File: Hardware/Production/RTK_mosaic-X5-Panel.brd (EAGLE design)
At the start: 151.8 x 101.6 mm, 350 parts, among them J2 MAGJACK-POE, J3 MICRO-SD-PUSH-PUSH-EXT-PIN, J4 Vertical Qwiic Connector, J9 MAGJACK-POE, U1 ESP32-WROVER-IE, U10 POE_PSU-DP990X, U11 SN74AVC4T774PW, U17 URB2405YMD, U2 CH340C, U3 XC6222B331MR-G, U4 TXS0108, U5 TXS0108, U6 XC6222B331MR-G, U7 KSZ8041NL, U8 MOSAIC-X5X5, U9 KSZ8041NL

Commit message: Tweaked and panelized
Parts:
- removed ACT, ACT2: JUMPER-SMT_2_NC_TRACE_SILK, SparkFun-Jumpers:SMT-JUMPER_2_NC_TRACE_SILK
- removed FRAME1: FRAME-LEDGER, SparkFun-Aesthetics:CREATIVE_COMMONS
- removed FRAME3: FRAME-LEDGERNO_FOOTPRINT, SparkFun-Aesthetics:DUMMY
- removed LOGO1: SPECIAL_INSTRUCTIONS-ORDERING, SparkFun-Aesthetics:ORDERING_INSTRUCTIONS
- removed U$100: (no value), output:MOSAIC_X50
- removed U$4: (no value), output:#LINK#1
- removed U$9: (no value), output:#ACT#0
- added E$1, E$2, E$3, E$4: (no value), SparkFun-Aesthetics:FIDUCIAL-1X2
- added E$5, E$6: (no value), SparkFun-Retired:FIDUCIAL-1.5X3
- added SPEED, SPEED2: JUMPER-SMT_2_NC_TRACE_SILK, SparkFun-Jumpers:SMT-JUMPER_2_NC_TRACE_SILK
- added U$109: (no value), output:#_BT_#1
- added U$110, U$116: (no value), output:#_LOG_#5
- added U$111: (no value), output:#_PVT_#3
- added U$112: (no value), output:#_RTK_#4
- added U$115: (no value), output:#_WIFI_#2
- added U$117: (no value), output:#_#RESET#_#0
- added U$118: (no value), output:#_BOOT_#1
- added U$119: (no value), output:#MOSAIC#8
- added U$120: (no value), output:#LINK#1
- added U$121, U$122: (no value), output:#SPEED#0
- U$2: device output:#ACT#0 -> output:MOSAIC#X50
- U$69, U$99: device output:RTK_MOSAIC_X50 -> output:RTK_MOSAIC#X50
- U3, U6: value XC6222B331MR-G -> AP7361C-33FGEUDFN-8; device SparkFun-IC-Power:SOT23-5 -> SparkFun-IC-Power:UDFN-8
- U8: device Septentrio_Mosaic:MOSAIC_LGA -> Septentrio_mosaic-X5:MOSAIC_LGA
- moved U$2 53.5 mm to (64.2, 97.0), flipped to the top, turned to 90 degrees
- moved U$10 11.9 mm to (131.6, 100.1)
- moved LINK 11.0 mm to (131.5, 98.4)
- moved LINK2 11.0 mm to (9.59, 98.4)
- moved U3 1.93 mm to (70.8, 45.1), turned to 90 degrees
- moved U6 1.93 mm to (70.8, 40.0), turned to 90 degrees
- moved FB3 1.43 mm to (60.6, 73.8)
- moved R39 1.31 mm to (35.2, 14.0)
- moved R36 1.31 mm to (10.5, 14.0)
- moved R28 1.31 mm to (18.7, 14.0)
- moved R38 1.31 mm to (27.0, 14.0)
- moved R27 1.31 mm to (52.4, 14.0)
- moved R37 1.31 mm to (43.5, 14.0)
- moved U$97 1.31 mm to (51.0, 66.9)
- moved D10 0.32 mm to (131.8, 11.4)
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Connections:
- net ACT_ESP32 renamed SPEED_ESP32
- net ACT_MOSAIC renamed SPEED_MOSAIC
- net N$13 renamed ESP32_RF
- removed net ACT: ACT.1, J9.14
- removed net ACT2: ACT2.1, J2.14
- removed net LINK: J9.12, LINK.1
- removed net LINK2: J2.12, LINK2.1
- new net N$3: J9.14, LINK.1
- new net N$40: J2.14, LINK2.1
- new net N$41: J2.12, SPEED2.1
- new net N$7: J9.12, SPEED.1
- net 3.3V: now also U6.1; no longer U6.5
- net 3.3V_SW: now also U3.1; no longer U3.5
- net 5V: now also U3.5, U3.8, U6.5, U6.8; no longer U3.1, U3.3, U6.1, U6.3
- net GND: now also U3.4, U3.EP, U6.4, U6.EP; no longer U3.2, U6.2
- net N$12: now also SPEED.2; no longer ACT.2
- net N$142: now also SPEED2.2; no longer ACT2.2
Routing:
- net N$143: track 21.7 -> 36.0 mm
- net N$21: track 41.5 -> 30.1 mm
- net N$12: track 29.8 -> 40.3 mm
- net N$142: track 34.1 -> 25.3 mm
- net GND: track 8.92 -> 17.6 mm, vias 204 -> 330
- net CH340-TXO: track 57.1 -> 60.8 mm
- net N$7: track 0.00 -> 3.32 mm
- net N$3: track 0.00 -> 3.30 mm
- net ACT: track 3.30 -> 0.00 mm
- net LINK: track 3.25 -> 0.00 mm
- net MOSAIC_LOG_BTN_IO: track 148.9 -> 151.7 mm
- net LINK2: track 2.48 -> 0.00 mm
- net N$40: track 0.00 -> 2.48 mm
- net N$41: track 0.00 -> 2.46 mm
- net ACT2: track 2.43 -> 0.00 mm
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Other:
- board size 151.8 x 101.6 mm -> 165.5 x 131.1 mm
- board text added: "Route Out"
- board text added: "v-score"
- board text removed: "Controlled Impedance: JLC7628 Material: TG155 4-Layers Thickness: 1.6mm Outer Copper: 1oz Inner Copper: 0.5oz Finish: ENIG Red Solder Resist White Silkscreen No clean process"
- board text removed: "Dimensions In Inches"
- board text removed: "Paul Clark"
- board text removed: "V-Score To V-Score"

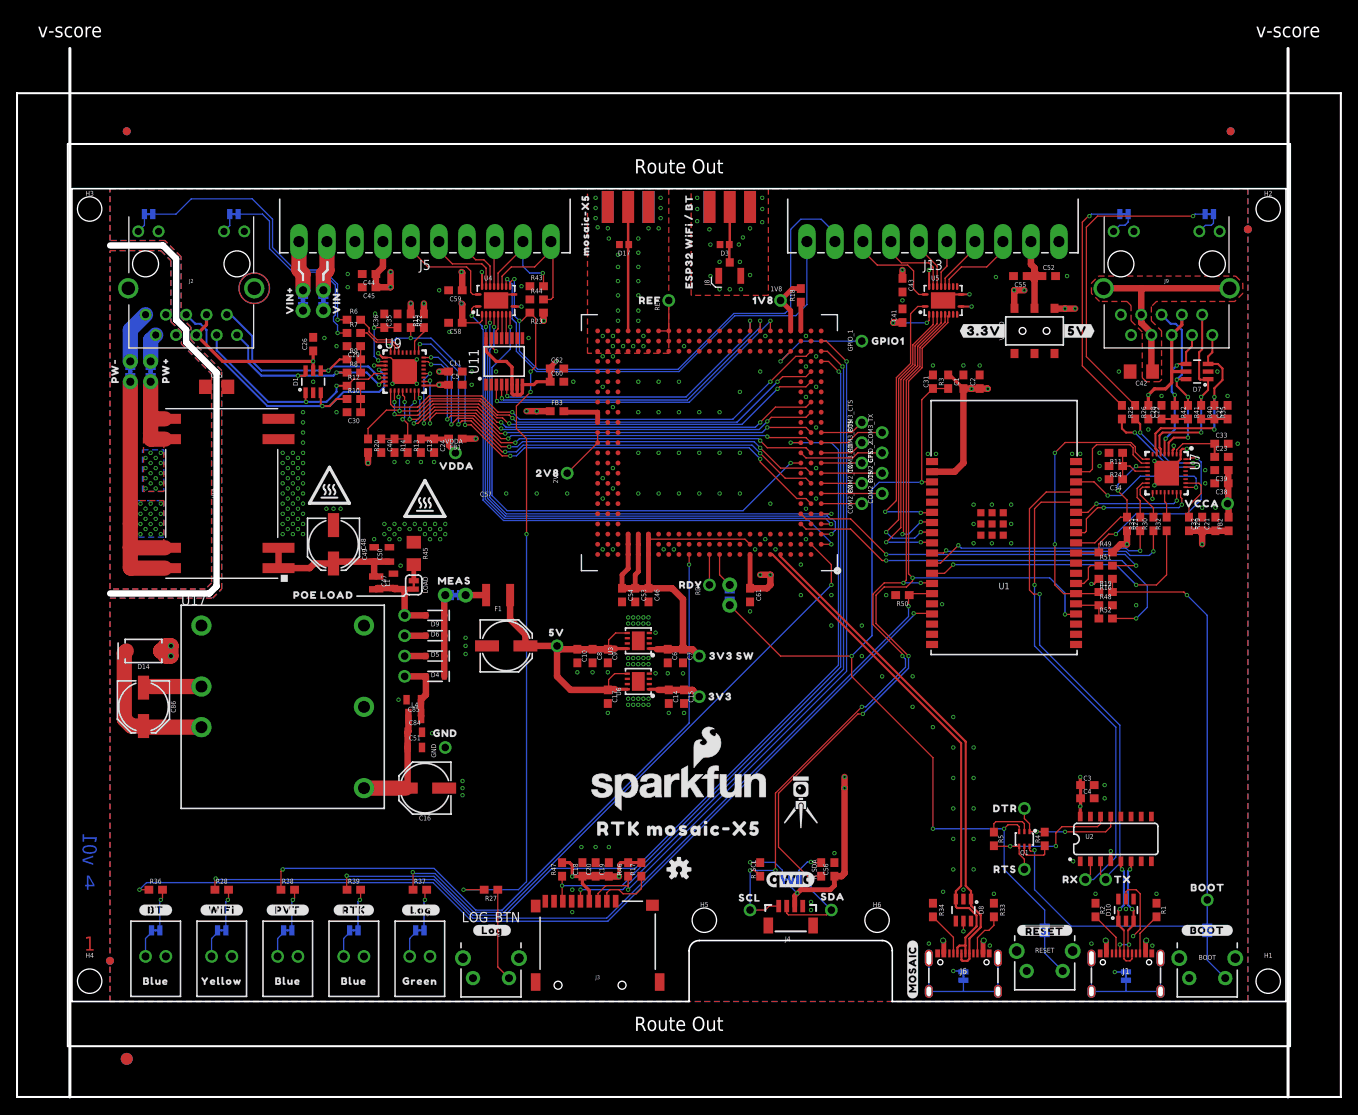
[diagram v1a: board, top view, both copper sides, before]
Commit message: Adding u.FL connector for mosaic-H - with standoff holes for a u.FL-SMA daughter board
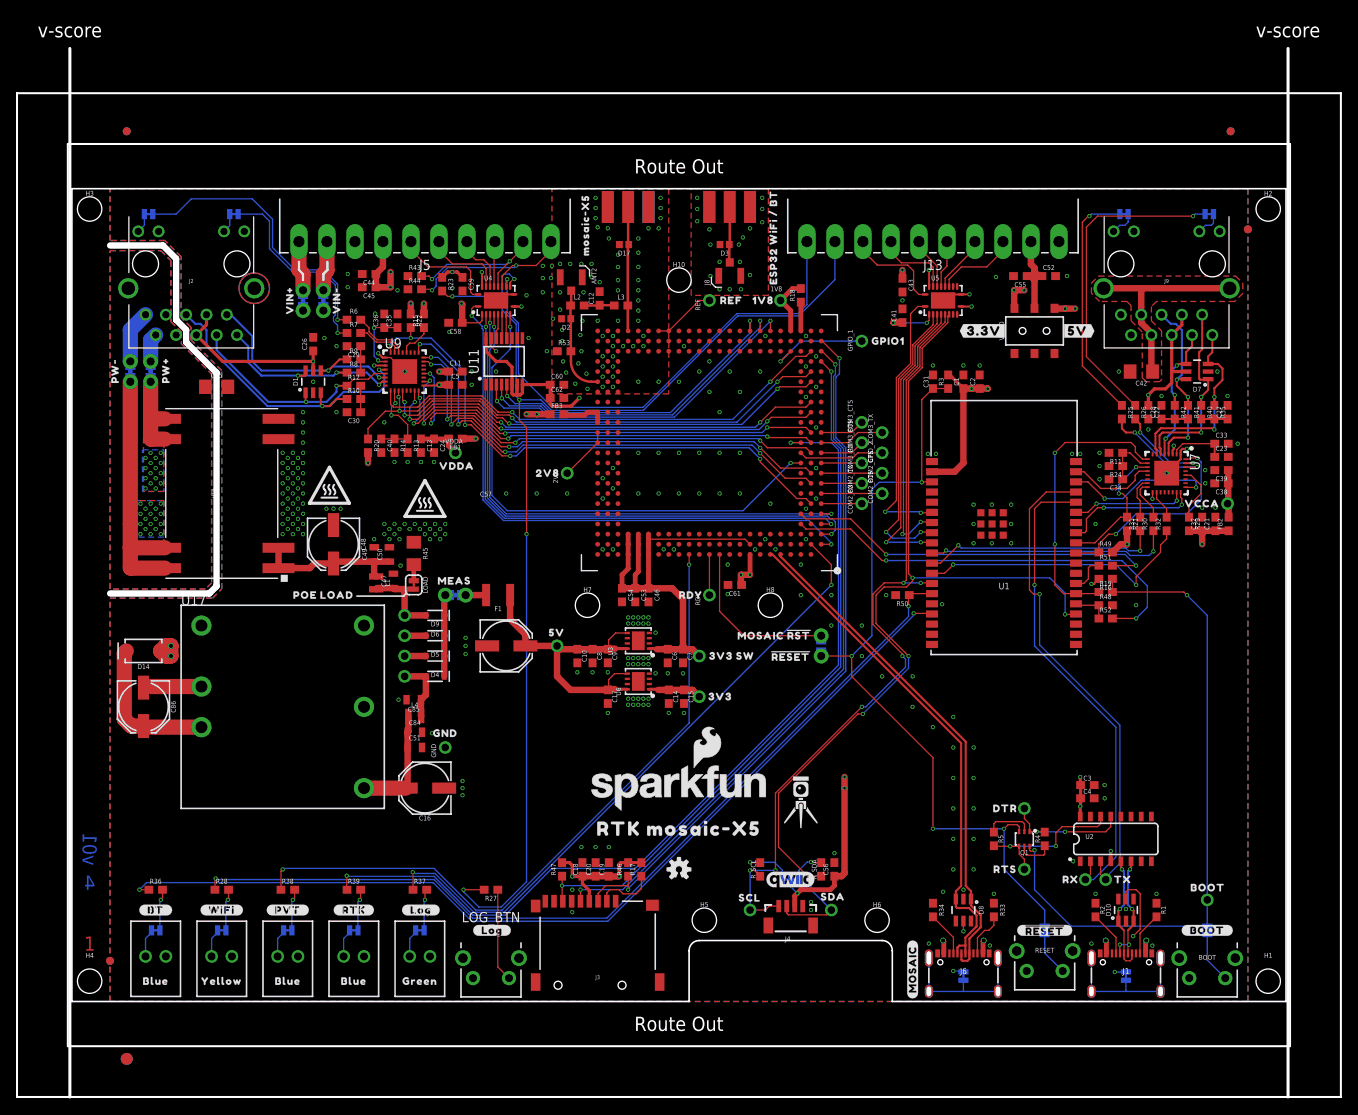
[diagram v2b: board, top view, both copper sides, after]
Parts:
- added ANT2: DNP, SparkFun-Connectors:U.FL_REDUCED_FOOTPRINT__NO_CREAM
- added C12: DNP, SparkFun-Capacitors:0603_NO_CREAM
- added D2: PESD0402, SparkFun-DiscreteSemi:0402
- added H10, H7, H8: STAND-OFFTIGHT, SparkFun-Hardware:STAND-OFF-TIGHT
- added L2, L3: DNP, SparkFun-Coils:0603_NO-CREAM
- added R53: 0, SparkFun-Resistors:0603
- added U$4: (no value), output:#RESET#0
- added U$9: (no value), output:MOSAIC_#RST#6
- U7, U9: device Septentrio_Mosaic:MLF55Q-32LD -> Septentrio_mosaic-X5:MLF55Q-32LD
- moved R43 15.3 mm to (42.9, 90.7)
- moved R44 15.3 mm to (42.9, 89.0)
- moved MOSAIC_RST 13.1 mm to (93.7, 44.5)
- moved R23 12.3 mm to (46.3, 89.7), turned to 270 degrees
- moved U$21 10.6 mm to (87.7, 102.1)
- moved U$79 10.2 mm to (84.5, 87.6)
- moved U$74 7.41 mm to (89.9, 43.2)
- moved U$73 6.35 mm to (82.6, 45.8)
- moved REF 5.08 mm to (79.7, 87.6)
- moved U$80 5.08 mm to (77.5, 86.1)
- moved C62 3.68 mm to (60.6, 75.4)
- moved C61 2.29 mm to (82.9, 52.1), turned to 180 degrees
- moved RDY 1.27 mm to (79.7, 50.8)
- moved U$75 1.27 mm to (79.6, 50.8)
- moved U$78 1.27 mm to (75.0, 50.8)
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- renumbered MOSAIC_RF to ANT1
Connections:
- net N$6 renamed VANT
- removed net MOSAIC_RF: ANT1.SIG, D17.1, U8.AC20
- new net ANT1: ANT1.SIG, D17.1, L3.2, U8.AC20
- new net ANT2: ANT2.FEED, D2.1, L2.1, R53.2, U8.V23
- new net N$13: C12.1, L2.2, L3.1
- net GND: now also ANT2.1, ANT2.2, C12.2, D2.2, R53.1; no longer U8.V23
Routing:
- net MOSAIC_!RST!: track 5.10 -> 21.8 mm
- net MOSAIC_RF: track 15.7 -> 0.00 mm
- net ANT1: track 0.00 -> 15.6 mm
- net !RESET!: track 114.4 -> 100.3 mm
- net ANT2: track 0.00 -> 13.3 mm
- net MOSAIC_EVENTB_IO: track 18.2 -> 23.5 mm, vias 0 -> 2
- net MOSAIC_PPSO_IO: track 59.1 -> 64.3 mm
- net 5V: track 183.7 -> 178.6 mm
- net VCCIO: track 130.1 -> 135.1 mm, vias 7 -> 6
- net MOSAIC_EVENTA_IO: track 14.5 -> 19.0 mm, vias 1 -> 2
- net N$13: track 0.00 -> 3.83 mm
- net REF: track 5.08 -> 7.93 mm
- net 1.8V: track 58.3 -> 60.6 mm
- net ESP23_MDC: track 13.3 -> 11.1 mm
- net MOSAIC_PPSO_1V8: track 38.0 -> 39.6 mm
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
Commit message: Add Phy PROD_ID. Ready for manufacture
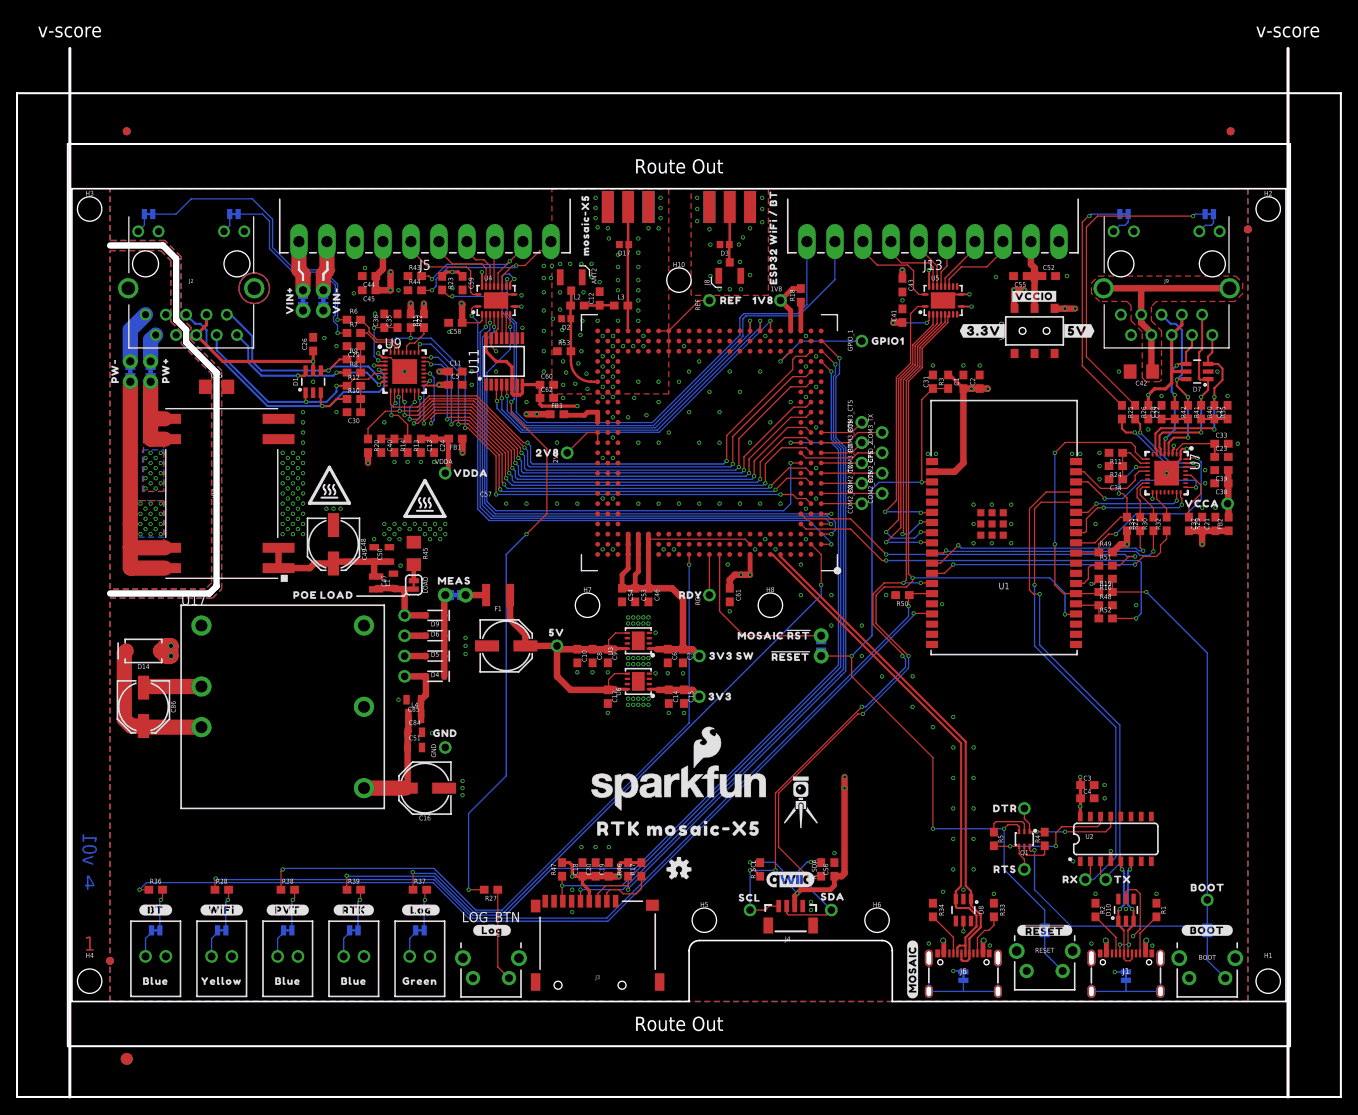
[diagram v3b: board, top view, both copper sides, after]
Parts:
- added U$100: (no value), output:#VCCIO#1
- U7, U9: value KSZ8041NL -> KSZ8041NLI
- moved VDDA 2.84 mm to (46.7, 66.0)
- moved 2V8 2.54 mm to (61.9, 68.6)
- moved U$41 2.54 mm to (61.7, 68.6)
- moved U$42 2.54 mm to (57.1, 68.6)
- moved U$97 1.99 mm to (52.8, 66.0)
- moved U$98 1.99 mm to (46.9, 66.0)
- moved C61 1.42 mm to (82.2, 50.8), turned to 270 degrees
- moved C60 1.27 mm to (59.4, 77.1)
- moved C62 1.27 mm to (59.4, 75.4)
- moved C45 0.38 mm to (37.1, 88.9)
- moved C44 0.25 mm to (37.1, 90.7)
- moved C59 0.13 mm to (48.8, 89.8)
- moved R23 0.13 mm to (46.3, 89.8)
- moved R44 0.13 mm to (42.9, 88.9)
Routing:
- net ETHER_CLK: track 59.7 -> 68.1 mm
- net ETHER_MDC: track 58.1 -> 66.2 mm
- net ETHER_MDIO: track 64.7 -> 72.4 mm
- net ETHER_CRSDV: track 57.5 -> 65.1 mm
- net ETHER_RXD0: track 57.0 -> 64.4 mm
- net ETHER_RXER: track 57.6 -> 65.0 mm
- net ETHER_RXD1: track 57.3 -> 64.4 mm
- net ETHER_TXEN: track 57.5 -> 64.1 mm
- net VCCIO: track 135.1 -> 141.0 mm
- net MOSAIC_PPSO_IO: track 64.3 -> 70.2 mm
- net MOSAIC_LOG_BTN: track 65.4 -> 69.7 mm
- net ETHER_TXD0: track 59.5 -> 63.1 mm
- net ETHER_TXD1: track 62.2 -> 65.0 mm
- net !BOOT!: track 83.2 -> 80.4 mm
- net ESP27_CRSDV: track 35.4 -> 32.7 mm
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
